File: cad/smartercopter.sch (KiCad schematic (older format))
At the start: 26 parts

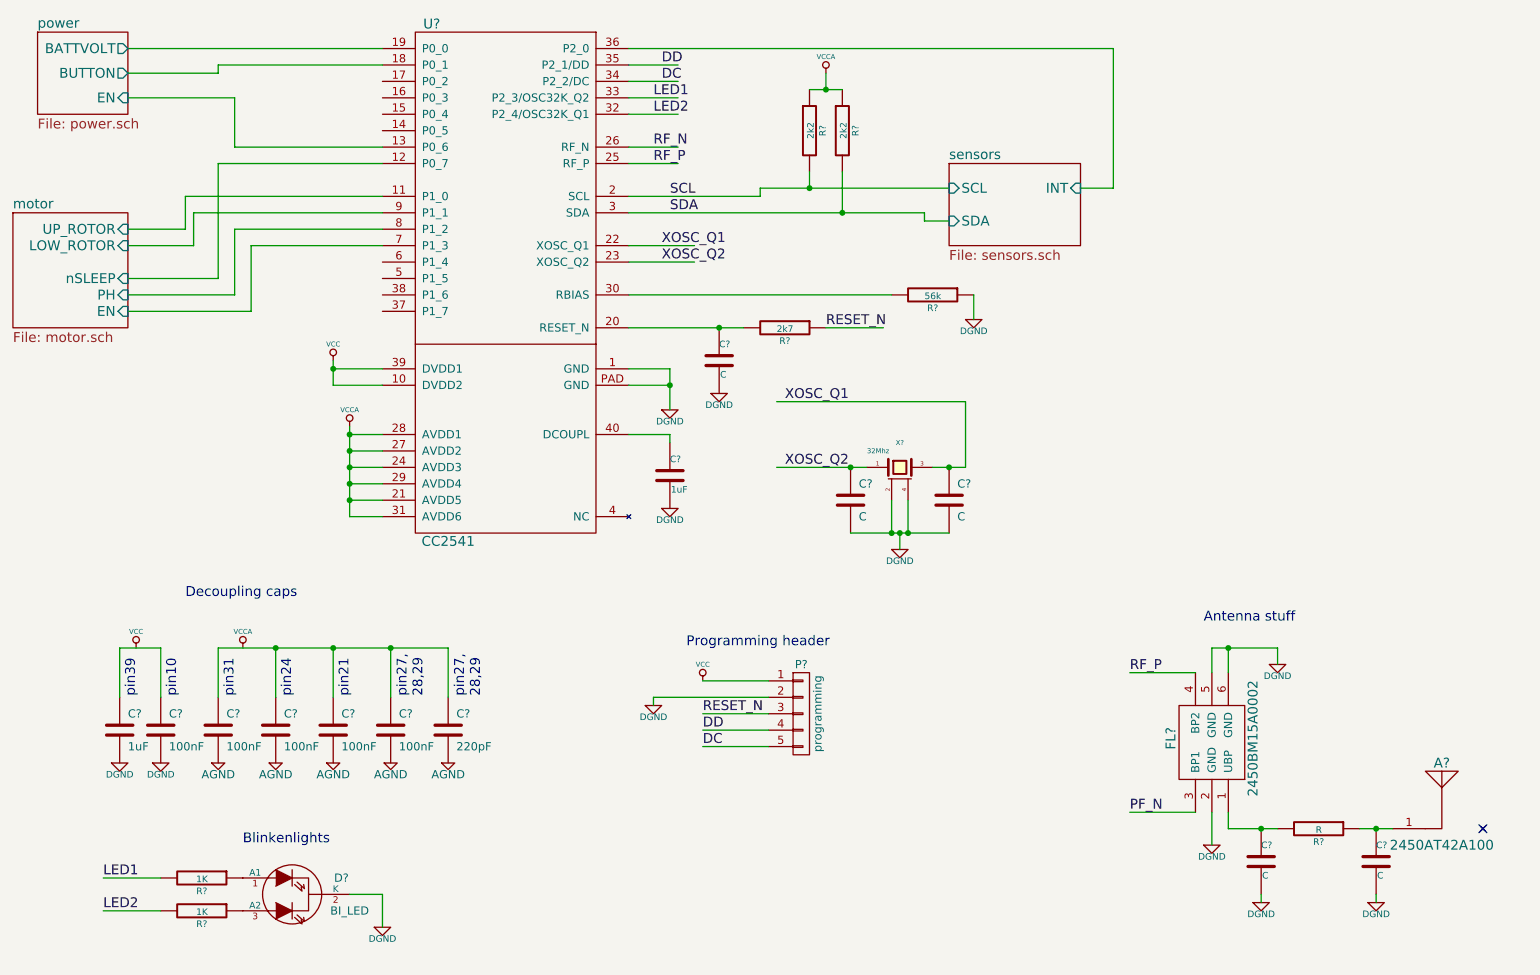
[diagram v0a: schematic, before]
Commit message: added values to crystal load caps
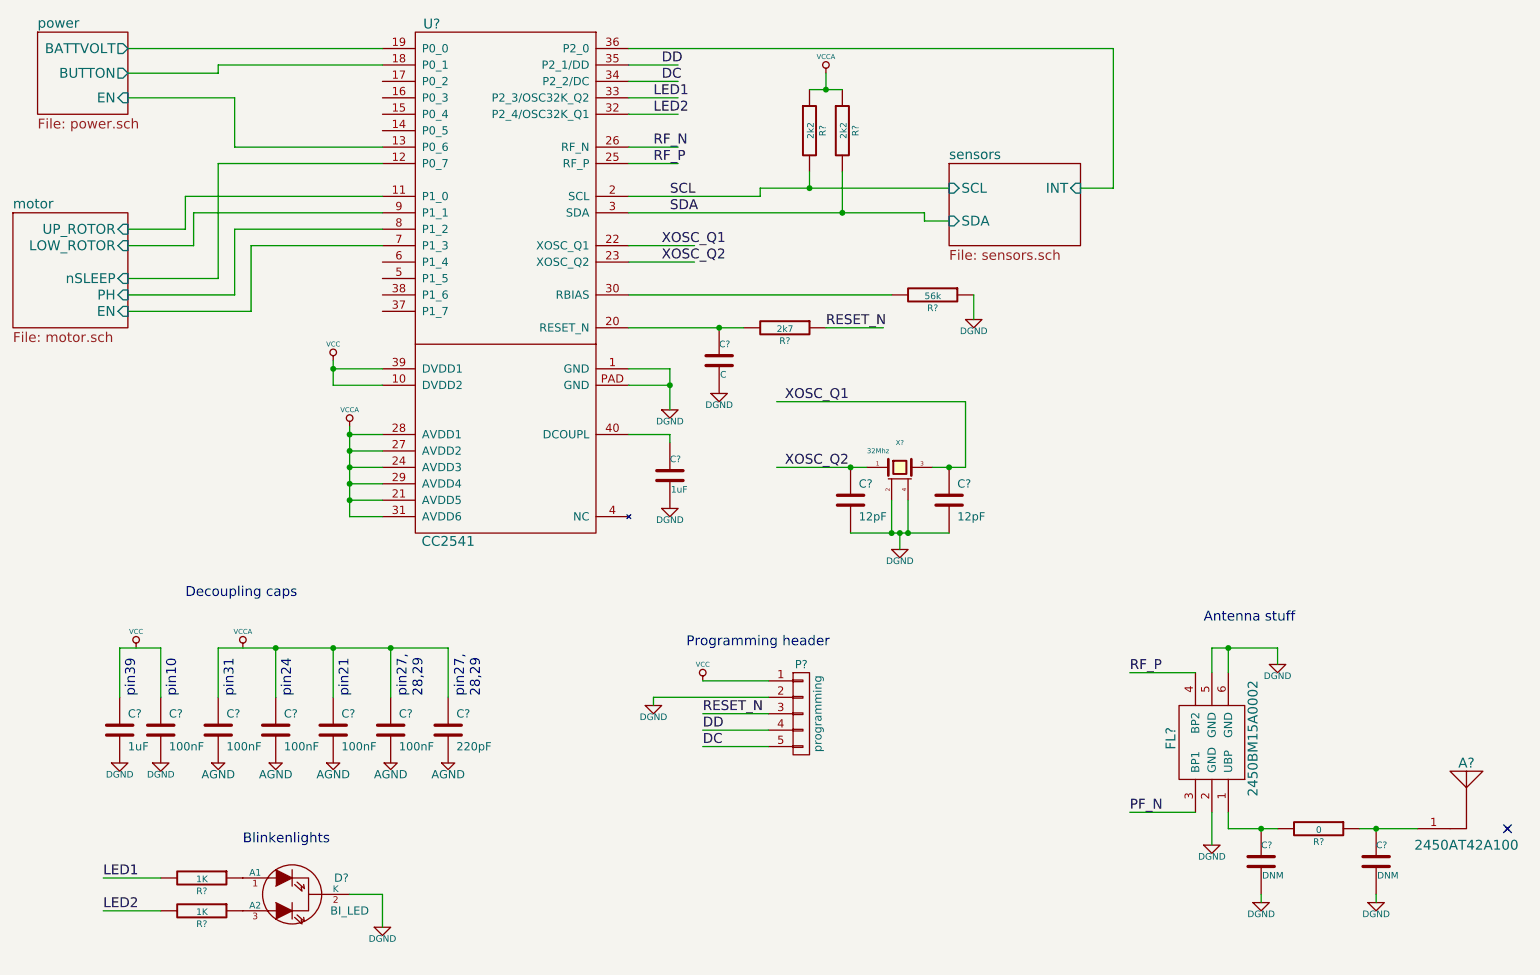
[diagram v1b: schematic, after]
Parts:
- C? (x2): value C -> 12pF
- C? (x2): value C -> DNM
- R?: value R -> 0
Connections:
- wire segments 101 -> 123
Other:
- moved on the sheet: A?
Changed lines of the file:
@@
 P 6800 4050
 F 0 "C?" H 6850 4150 50  0000 L CNN
-F 1 "C" H 6850 3950 50  0000 L CNN
+F 1 "12pF" H 6850 3950 50  0000 L CNN
 F 2 "" H 6800 4050 60  0000 C CNN
 F 3 "" H 6800 4050 60  0000 C CNN
@@
 P 6200 4050
 F 0 "C?" H 6250 4150 50  0000 L CNN
-F 1 "C" H 6250 3950 50  0000 L CNN
+F 1 "12pF" H 6250 3950 50  0000 L CNN
 F 2 "" H 6200 4050 60  0000 C CNN
 F 3 "" H 6200 4050 60  0000 C CNN
@@
 $EndComp
 Wire Wire Line
-	3150 3600 3150 4150
+	3150 3600 3150 3650
+Wire Wire Line
+	3150 3650 3150 3750
+Wire Wire Line
+	3150 3750 3150 3850
+Wire Wire Line
+	3150 3850 3150 3950
+Wire Wire Line
+	3150 3950 3150 4050
+Wire Wire Line
+	3150 4050 3150 4150
 Wire Wire Line
 	3150 4150 3350 4150
@@
 	4850 3250 5100 3250
 Wire Wire Line
-	5100 3250 5100 3500
+	5100 3250 5100 3350
+Wire Wire Line
+	5100 3350 5100 3500
 Wire Wire Line
 	4850 3350 5100 3350
 Connection ~ 5100 3350
 Wire Wire Line
-	3050 3200 3050 3350
+	3050 3200 3050 3250
+Wire Wire Line
+	3050 3250 3050 3350
 Wire Wire Line
 	4850 3650 5100 3650
@@
 	5100 3650 5100 3700
 Wire Wire Line
-	4850 3000 5550 3000
+	4850 3000 5400 3000
+Wire Wire Line
+	5400 3000 5550 3000
 Connection ~ 5400 3000
 Wire Wire Line
@@
 	6950 2800 6950 2950
 Wire Wire Line
-	6200 4250 6800 4250
+	6200 4250 6450 4250
+Wire Wire Line
+	6450 4250 6500 4250
+Wire Wire Line
+	6500 4250 6550 4250
+Wire Wire Line
+	6550 4250 6800 4250
 Wire Wire Line
 	6550 4050 6550 4250
@@
 	4850 2200 5650 2200
 Wire Wire Line
-	4850 2300 6650 2300
+	4850 2300 6150 2300
+Wire Wire Line
+	6150 2300 6650 2300
 Text Label 5100 2200 0    60   ~ 0
 SCL
@@
 XOSC_Q2
 Wire Wire Line
-	5750 3850 6300 3850
-Wire Wire Line
-	6700 3850 6900 3850
+	5750 3850 6200 3850
+Wire Wire Line
+	6200 3850 6300 3850
+Wire Wire Line
+	6700 3850 6800 3850
+Wire Wire Line
+	6800 3850 6900 3850
 Wire Wire Line
 	6900 3850 6900 3450
@@
 	2350 5250 2350 4950
 Wire Wire Line
-	2350 4950 3750 4950
+	2350 4950 2700 4950
+Wire Wire Line
+	2700 4950 3050 4950
+Wire Wire Line
+	3050 4950 3400 4950
+Wire Wire Line
+	3400 4950 3750 4950
 Wire Wire Line
 	3750 4950 3750 5250
@@
 	5650 2200 5650 2150
 Wire Wire Line
-	5650 2150 6800 2150
+	5650 2150 5950 2150
+Wire Wire Line
+	5950 2150 6800 2150
 Wire Wire Line
 	6650 2300 6650 2350
@@
 $EndComp
 Wire Wire Line
-	5950 1550 6150 1550
+	5950 1550 6050 1550
+Wire Wire Line
+	6050 1550 6150 1550
 Wire Wire Line
 	6050 1450 6050 1550
@@
 L 2450AT42A100 A?
 U 1 1 54954E38
-P 9800 6050
-F 0 "A?" H 9800 6450 60  0000 C CNN
-F 1 "2450AT42A100" H 9800 5950 60  0000 C CNN
-F 2 "" H 9800 6050 60  0000 C CNN
-F 3 "" H 9800 6050 60  0000 C CNN
-	1    9800 6050
+P 9950 6050
+F 0 "A?" H 9950 6450 60  0000 C CNN
+F 1 "2450AT42A100" H 9950 5950 60  0000 C CNN
+F 2 "" H 9950 6050 60  0000 C CNN
+F 3 "" H 9950 6050 60  0000 C CNN
+	1    9950 6050
 	1    0    0    -1
 $EndComp
@@
 P 8700 6250
 F 0 "C?" H 8700 6350 40  0000 L CNN
-F 1 "C" H 8706 6165 40  0000 L CNN
+F 1 "DNM" H 8706 6165 40  0000 L CNN
 F 2 "" H 8738 6100 30  0000 C CNN
 F 3 "" H 8700 6250 60  0000 C CNN
@@
 P 9400 6250
 F 0 "C?" H 9400 6350 40  0000 L CNN
-F 1 "C" H 9406 6165 40  0000 L CNN
+F 1 "DNM" H 9406 6165 40  0000 L CNN
 F 2 "" H 9438 6100 30  0000 C CNN
 F 3 "" H 9400 6250 60  0000 C CNN
@@
 P 9050 6050
 F 0 "R?" V 9130 6050 40  0000 C CNN
-F 1 "R" V 9057 6051 40  0000 C CNN
+F 1 "0" V 9057 6051 40  0000 C CNN
 F 2 "" V 8980 6050 30  0000 C CNN
 F 3 "" H 9050 6050 30  0000 C CNN
@@
 $EndComp
 $Comp
-L DGND #PWR?
+L DGND #PWR018
 U 1 1 5495965C
 P 8400 6150
-F 0 "#PWR?" H 8400 6150 40  0001 C CNN
+F 0 "#PWR018" H 8400 6150 40  0001 C CNN
 F 1 "DGND" H 8400 6080 40  0000 C CNN
 F 2 "" H 8400 6150 60  0000 C CNN
@@
 $EndComp
 $Comp
-L DGND #PWR?
+L DGND #PWR019
 U 1 1 549596DE
 P 9400 6500
-F 0 "#PWR?" H 9400 6500 40  0001 C CNN
+F 0 "#PWR019" H 9400 6500 40  0001 C CNN
 F 1 "DGND" H 9400 6430 40  0000 C CNN
 F 2 "" H 9400 6500 60  0000 C CNN
@@
 $EndComp
 $Comp
-L DGND #PWR?
+L DGND #PWR020
 U 1 1 54959760
 P 8800 5050
-F 0 "#PWR?" H 8800 5050 40  0001 C CNN
+F 0 "#PWR020" H 8800 5050 40  0001 C CNN
 F 1 "DGND" H 8800 4980 40  0000 C CNN
 F 2 "" H 8800 5050 60  0000 C CNN
@@
 $EndComp
 $Comp
-L DGND #PWR?
+L DGND #PWR021
 U 1 1 54959F9E
 P 8700 6500
-F 0 "#PWR?" H 8700 6500 40  0001 C CNN
+F 0 "#PWR021" H 8700 6500 40  0001 C CNN
 F 1 "DGND" H 8700 6430 40  0000 C CNN
 F 2 "" H 8700 6500 60  0000 C CNN
@@
 $EndComp
 Wire Wire Line
-	8500 6050 8800 6050
-Wire Wire Line
-	9300 6050 9500 6050
+	8500 6050 8700 6050
+Wire Wire Line
+	8700 6050 8800 6050
+Wire Wire Line
+	9300 6050 9400 6050
+Wire Wire Line
+	9400 6050 9650 6050
 Connection ~ 9400 6050
 Wire Wire Line
@@
 Wire Wire Line
 	8700 6500 8700 6450
-NoConn ~ 10050 6050
+NoConn ~ 10200 6050
 Wire Wire Line
 	8500 5950 8500 6050
@@
 	8400 5100 8400 4950
 Wire Wire Line
-	8400 4950 8800 4950
+	8400 4950 8500 4950
+Wire Wire Line
+	8500 4950 8800 4950
 Wire Wire Line
 	8800 4950 8800 5050
@@
 $EndComp
 $Comp
-L DGND #PWR?
+L DGND #PWR022
 U 1 1 549158BD
 P 3350 6650
-F 0 "#PWR?" H 3350 6650 40  0001 C CNN
+F 0 "#PWR022" H 3350 6650 40  0001 C CNN
 F 1 "DGND" H 3350 6580 40  0000 C CNN
 F 2 "" H 3350 6650 60  0000 C CNN
@@
 	5700 5450 5300 5450
 $Comp
-L VCC #PWR?
+L VCC #PWR023
 U 1 1 549191D8
 P 5300 5150
-F 0 "#PWR?" H 5300 5250 30  0001 C CNN
+F 0 "#PWR023" H 5300 5250 30  0001 C CNN
 F 1 "VCC" H 5300 5250 30  0000 C CNN
 F 2 "" H 5300 5150 60  0000 C CNN
@@
 $EndComp
 $Comp
-L DGND #PWR?
+L DGND #PWR024
 U 1 1 54919227
 P 5000 5300
-F 0 "#PWR?" H 5000 5300 40  0001 C CNN
+F 0 "#PWR024" H 5000 5300 40  0001 C CNN
 F 1 "DGND" H 5000 5230 40  0000 C CNN
 F 2 "" H 5000 5300 60  0000 C CNN

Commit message: passed erc
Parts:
- gave numbers to parts that had none: 26
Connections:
- net labels removed: PF_N
- wire segments 123 -> 101
- no-connect marks 1 -> 9
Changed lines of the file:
@@
 $EndDescr
 $Comp
-L CC2541 U?
+L CC2541 U1
 U 1 1 548BD357
 P 4100 2650
-F 0 "U?" H 3650 4150 60  0000 C CNN
+F 0 "U1" H 3650 4150 60  0000 C CNN
 F 1 "CC2541" H 3750 1000 60  0000 C CNN
 F 2 "" H 4500 1250 60  0000 C CNN
@@
 $EndSheet
 $Comp
-L C C?
+L C C8
 U 1 1 548CB6FE
 P 5100 3900
-F 0 "C?" H 5100 4000 40  0000 L CNN
+F 0 "C8" H 5100 4000 40  0000 L CNN
 F 1 "1uF" H 5106 3815 40  0000 L CNN
 F 2 "" H 5138 3750 30  0000 C CNN
@@
 $EndComp
 $Comp
-L C C?
+L C C9
 U 1 1 548CC96E
 P 5400 3200
-F 0 "C?" H 5400 3300 40  0000 L CNN
+F 0 "C9" H 5400 3300 40  0000 L CNN
 F 1 "C" H 5406 3115 40  0000 L CNN
 F 2 "" H 5438 3050 30  0000 C CNN
@@
 $EndComp
 $Comp
-L R R?
+L R R3
 U 1 1 548CCA9E
 P 5800 3000
-F 0 "R?" V 5880 3000 40  0000 C CNN
+F 0 "R3" V 5880 3000 40  0000 C CNN
 F 1 "2k7" V 5807 3001 40  0000 C CNN
 F 2 "" V 5730 3000 30  0000 C CNN
@@
 RESET_N
 $Comp
-L R R?
+L R R6
 U 1 1 548CCFA8
 P 6700 2800
-F 0 "R?" V 6780 2800 40  0000 C CNN
+F 0 "R6" V 6780 2800 40  0000 C CNN
 F 1 "56k" V 6707 2801 40  0000 C CNN
 F 2 "" V 6630 2800 30  0000 C CNN
@@
 $EndComp
 $Comp
-L C C?
+L C C11
 U 1 1 548CD35A
 P 6800 4050
-F 0 "C?" H 6850 4150 50  0000 L CNN
+F 0 "C11" H 6850 4150 50  0000 L CNN
 F 1 "12pF" H 6850 3950 50  0000 L CNN
 F 2 "" H 6800 4050 60  0000 C CNN
@@
 $EndComp
 $Comp
-L C C?
+L C C10
 U 1 1 548CD39E
 P 6200 4050
-F 0 "C?" H 6250 4150 50  0000 L CNN
+F 0 "C10" H 6250 4150 50  0000 L CNN
 F 1 "12pF" H 6250 3950 50  0000 L CNN
 F 2 "" H 6200 4050 60  0000 C CNN
@@
 $EndComp
 Wire Wire Line
-	3150 3600 3150 3650
-Wire Wire Line
-	3150 3650 3150 3750
-Wire Wire Line
-	3150 3750 3150 3850
-Wire Wire Line
-	3150 3850 3150 3950
-Wire Wire Line
-	3150 3950 3150 4050
-Wire Wire Line
-	3150 4050 3150 4150
+	3150 3600 3150 4150
 Wire Wire Line
 	3150 4150 3350 4150
@@
 	4850 3250 5100 3250
 Wire Wire Line
-	5100 3250 5100 3350
-Wire Wire Line
-	5100 3350 5100 3500
+	5100 3250 5100 3500
 Wire Wire Line
 	4850 3350 5100 3350
 Connection ~ 5100 3350
 Wire Wire Line
-	3050 3200 3050 3250
-Wire Wire Line
-	3050 3250 3050 3350
+	3050 3200 3050 3350
 Wire Wire Line
 	4850 3650 5100 3650
@@
 	5100 3650 5100 3700
 Wire Wire Line
-	4850 3000 5400 3000
-Wire Wire Line
-	5400 3000 5550 3000
+	4850 3000 5550 3000
 Connection ~ 5400 3000
 Wire Wire Line
@@
 	6950 2800 6950 2950
 Wire Wire Line
-	6200 4250 6450 4250
-Wire Wire Line
-	6450 4250 6500 4250
-Wire Wire Line
-	6500 4250 6550 4250
-Wire Wire Line
-	6550 4250 6800 4250
+	6200 4250 6800 4250
 Wire Wire Line
 	6550 4050 6550 4250
@@
 	4850 2200 5650 2200
 Wire Wire Line
-	4850 2300 6150 2300
-Wire Wire Line
-	6150 2300 6650 2300
+	4850 2300 6650 2300
 Text Label 5100 2200 0    60   ~ 0
 SCL
@@
 XOSC_Q2
 Wire Wire Line
-	5750 3850 6200 3850
-Wire Wire Line
-	6200 3850 6300 3850
-Wire Wire Line
-	6700 3850 6800 3850
-Wire Wire Line
-	6800 3850 6900 3850
+	5750 3850 6300 3850
+Wire Wire Line
+	6700 3850 6900 3850
 Wire Wire Line
 	6900 3850 6900 3450
@@
 XOSC_Q2
 $Comp
-L C C?
+L C C1
 U 1 1 548D168D
 P 1750 5450
-F 0 "C?" H 1800 5550 50  0000 L CNN
+F 0 "C1" H 1800 5550 50  0000 L CNN
 F 1 "1uF" H 1800 5350 50  0000 L CNN
 F 2 "" H 1750 5450 60  0000 C CNN
@@
 $EndComp
 $Comp
-L C C?
+L C C2
 U 1 1 548D1805
 P 2000 5450
-F 0 "C?" H 2050 5550 50  0000 L CNN
+F 0 "C2" H 2050 5550 50  0000 L CNN
 F 1 "100nF" H 2050 5350 50  0000 L CNN
 F 2 "" H 2000 5450 60  0000 C CNN
@@
 $EndComp
 $Comp
-L C C?
+L C C3
 U 1 1 548D182C
 P 2350 5450
-F 0 "C?" H 2400 5550 50  0000 L CNN
+F 0 "C3" H 2400 5550 50  0000 L CNN
 F 1 "100nF" H 2400 5350 50  0000 L CNN
 F 2 "" H 2350 5450 60  0000 C CNN
@@
 $EndComp
 $Comp
-L C C?
+L C C4
 U 1 1 548D1892
 P 2700 5450
-F 0 "C?" H 2750 5550 50  0000 L CNN
+F 0 "C4" H 2750 5550 50  0000 L CNN
 F 1 "100nF" H 2750 5350 50  0000 L CNN
 F 2 "" H 2700 5450 60  0000 C CNN
@@
 $EndComp
 $Comp
-L C C?
+L C C5
 U 1 1 548D18DD
 P 3050 5450
-F 0 "C?" H 3100 5550 50  0000 L CNN
+F 0 "C5" H 3100 5550 50  0000 L CNN
 F 1 "100nF" H 3100 5350 50  0000 L CNN
 F 2 "" H 3050 5450 60  0000 C CNN
@@
 $EndComp
 $Comp
-L C C?
+L C C6
 U 1 1 548D1913
 P 3400 5450
-F 0 "C?" H 3450 5550 50  0000 L CNN
+F 0 "C6" H 3450 5550 50  0000 L CNN
 F 1 "100nF" H 3450 5350 50  0000 L CNN
 F 2 "" H 3400 5450 60  0000 C CNN
@@
 $EndComp
 $Comp
-L C C?
+L C C7
 U 1 1 548D1948
 P 3750 5450
-F 0 "C?" H 3800 5550 50  0000 L CNN
+F 0 "C7" H 3800 5550 50  0000 L CNN
 F 1 "220pF" H 3800 5350 50  0000 L CNN
 F 2 "" H 3750 5450 60  0000 C CNN
@@
 	2350 5250 2350 4950
 Wire Wire Line
-	2350 4950 2700 4950
-Wire Wire Line
-	2700 4950 3050 4950
-Wire Wire Line
-	3050 4950 3400 4950
-Wire Wire Line
-	3400 4950 3750 4950
+	2350 4950 3750 4950
 Wire Wire Line
 	3750 4950 3750 5250
@@
 	5650 2200 5650 2150
 Wire Wire Line
-	5650 2150 5950 2150
-Wire Wire Line
-	5950 2150 6800 2150
+	5650 2150 6800 2150
 Wire Wire Line
 	6650 2300 6650 2350
@@
 	6650 2350 6800 2350
 $Comp
-L R R?
+L R R4
 U 1 1 549350E6
 P 5950 1800
-F 0 "R?" V 6030 1800 40  0000 C CNN
+F 0 "R4" V 6030 1800 40  0000 C CNN
 F 1 "2k2" V 5957 1801 40  0000 C CNN
 F 2 "" V 5880 1800 30  0000 C CNN
@@
 $EndComp
 $Comp
-L R R?
+L R R5
 U 1 1 5493575D
 P 6150 1800
-F 0 "R?" V 6230 1800 40  0000 C CNN
+F 0 "R5" V 6230 1800 40  0000 C CNN
 F 1 "2k2" V 6157 1801 40  0000 C CNN
 F 2 "" V 6080 1800 30  0000 C CNN
@@
 $EndComp
 Wire Wire Line
-	5950 1550 6050 1550
-Wire Wire Line
-	6050 1550 6150 1550
+	5950 1550 6150 1550
 Wire Wire Line
 	6050 1450 6050 1550
@@
 	7800 2150 7600 2150
 $Comp
-L CRYSTAL_SMD_2GND X?
+L CRYSTAL_SMD_2GND X1
 U 1 1 54948988
 P 6500 3850
-F 0 "X?" H 6500 4000 30  0000 C CNN
+F 0 "X1" H 6500 4000 30  0000 C CNN
 F 1 "32Mhz" H 6300 3950 30  0000 L CNN
 F 2 "" H 6500 3850 60  0000 C CNN
@@
 	1800 2900 2550 2900
 $Comp
-L 2450BM15A0002 FL?
+L 2450BM15A0002 FL1
 U 1 1 54954D1C
 P 8400 5550
-F 0 "FL?" H 8450 5800 60  0000 C CNN
+F 0 "FL1" H 8450 5800 60  0000 C CNN
 F 1 "2450BM15A0002" H 8450 5300 60  0000 C CNN
 F 2 "" H 8500 5350 60  0000 C CNN
@@
 $EndComp
 $Comp
-L 2450AT42A100 A?
+L 2450AT42A100 A1
 U 1 1 54954E38
 P 9950 6050
-F 0 "A?" H 9950 6450 60  0000 C CNN
+F 0 "A1" H 9950 6450 60  0000 C CNN
 F 1 "2450AT42A100" H 9950 5950 60  0000 C CNN
 F 2 "" H 9950 6050 60  0000 C CNN
@@
 RF_P
 Text Label 7900 5950 0    60   ~ 0
-PF_N
-$Comp
-L C C?
+RF_N
+$Comp
+L C C12
 U 1 1 54959458
 P 8700 6250
-F 0 "C?" H 8700 6350 40  0000 L CNN
+F 0 "C12" H 8700 6350 40  0000 L CNN
 F 1 "DNM" H 8706 6165 40  0000 L CNN
 F 2 "" H 8738 6100 30  0000 C CNN
@@
 $EndComp
 $Comp
-L C C?
+L C C13
 U 1 1 549594ED
 P 9400 6250
-F 0 "C?" H 9400 6350 40  0000 L CNN
+F 0 "C13" H 9400 6350 40  0000 L CNN
 F 1 "DNM" H 9406 6165 40  0000 L CNN
 F 2 "" H 9438 6100 30  0000 C CNN
@@
 $EndComp
 $Comp
-L R R?
+L R R7
 U 1 1 5495957A
 P 9050 6050
-F 0 "R?" V 9130 6050 40  0000 C CNN
+F 0 "R7" V 9130 6050 40  0000 C CNN
 F 1 "0" V 9057 6051 40  0000 C CNN
 F 2 "" V 8980 6050 30  0000 C CNN
@@
 $EndComp
 Wire Wire Line
-	8500 6050 8700 6050
-Wire Wire Line
-	8700 6050 8800 6050
-Wire Wire Line
-	9300 6050 9400 6050
-Wire Wire Line
-	9400 6050 9650 6050
+	8500 6050 8800 6050
+Wire Wire Line
+	9300 6050 9650 6050
 Connection ~ 9400 6050
 Wire Wire Line
@@
 	8400 5100 8400 4950
 Wire Wire Line
-	8400 4950 8500 4950
-Wire Wire Line
-	8500 4950 8800 4950
+	8400 4950 8800 4950
 Wire Wire Line
 	8800 4950 8800 5050
@@
 LED2
 $Comp
-L R R?
+L R R1
 U 1 1 5491496C
 P 2250 6350
-F 0 "R?" V 2330 6350 40  0000 C CNN
+F 0 "R1" V 2330 6350 40  0000 C CNN
 F 1 "1K" V 2257 6351 40  0000 C CNN
 F 2 "" V 2180 6350 30  0000 C CNN
@@
 $EndComp
 $Comp
-L BI_LED D?
+L BI_LED D1
 U 1 1 549157A0
 P 2800 6450
-F 0 "D?" H 3100 6550 50  0000 C CNN
+F 0 "D1" H 3100 6550 50  0000 C CNN
 F 1 "BI_LED" H 3150 6350 50  0000 C CNN
 F 2 "" H 2800 6450 60  0000 C CNN
@@
 $EndComp
 $Comp
-L R R?
+L R R2
 U 1 1 54915854
 P 2250 6550
-F 0 "R?" V 2330 6550 40  0000 C CNN
+F 0 "R2" V 2330 6550 40  0000 C CNN
 F 1 "1K" V 2257 6551 40  0000 C CNN
 F 2 "" V 2180 6550 30  0000 C CNN
@@
 LED2
 $Comp
-L CONN_01X05 P?
+L CONN_01X05 P1
 U 1 1 5491875F
 P 5900 5350
-F 0 "P?" H 5900 5650 50  0000 C CNN
+F 0 "P1" H 5900 5650 50  0000 C CNN
 F 1 "programming" V 6000 5350 50  0000 C CNN
 F 2 "" H 5900 5350 60  0000 C CNN
@@
 Text Notes 2150 4650 0    60   ~ 0
 Decoupling caps
+NoConn ~ 3350 1500
+NoConn ~ 3350 1600
+NoConn ~ 3350 1700
+NoConn ~ 3350 1800
+NoConn ~ 3350 2600
+NoConn ~ 3350 2700
+NoConn ~ 3350 2800
+NoConn ~ 3350 2900
 $EndSCHEMATC

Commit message: did stuff here, not exactly sure what
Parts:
- C2: MPN (none) -> LMK105BJ104KV-F
- C9: value C -> 1nF
- P1: value programming -> CONN_5
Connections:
- no-connect marks 9 -> 8
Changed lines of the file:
@@
 P 5400 3200
 F 0 "C9" H 5400 3300 40  0000 L CNN
-F 1 "C" H 5406 3115 40  0000 L CNN
+F 1 "1nF" H 5406 3115 40  0000 L CNN
 F 2 "" H 5438 3050 30  0000 C CNN
 F 3 "" H 5400 3200 60  0000 C CNN
@@
 F 2 "" H 2000 5450 60  0000 C CNN
 F 3 "" H 2000 5450 60  0000 C CNN
+F 4 "LMK105BJ104KV-F" H 2000 5450 60  0001 C CNN "MPN"
 	1    2000 5450
 	1    0    0    -1
@@
 Wire Wire Line
 	8700 6500 8700 6450
-NoConn ~ 10200 6050
 Wire Wire Line
 	8500 5950 8500 6050
@@
 P 5900 5350
 F 0 "P1" H 5900 5650 50  0000 C CNN
-F 1 "programming" V 6000 5350 50  0000 C CNN
+F 1 "CONN_5" V 6000 5350 50  0000 C CNN
 F 2 "" H 5900 5350 60  0000 C CNN
 F 3 "" H 5900 5350 60  0000 C CNN

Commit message: added more stuff to bom
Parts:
- A1: MPN (none) -> 2450AT42A100
- C1: MPN (none) -> GRM155R60J105KE19D
- C10: MPN (none) -> 02013A120JAT2A
- FL1: MPN (none) -> 2450BM15A0002
- X1: MPN (none) -> FA-128 32MHz 10pF 10PPM
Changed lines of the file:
@@
 F 2 "" H 6200 4050 60  0000 C CNN
 F 3 "" H 6200 4050 60  0000 C CNN
+F 4 "02013A120JAT2A" H 6200 4050 60  0001 C CNN "MPN"
 	1    6200 4050
 	1    0    0    -1
@@
 F 2 "" H 1750 5450 60  0000 C CNN
 F 3 "" H 1750 5450 60  0000 C CNN
+F 4 "GRM155R60J105KE19D" H 1750 5450 60  0001 C CNN "MPN"
 	1    1750 5450
 	1    0    0    -1
@@
 F 2 "" H 6500 3850 60  0000 C CNN
 F 3 "" H 6500 3850 60  0000 C CNN
+F 4 "FA-128 32MHz 10pF 10PPM" H 6500 3850 60  0001 C CNN "MPN"
 	1    6500 3850
 	1    0    0    -1
@@
 F 2 "" H 8500 5350 60  0000 C CNN
 F 3 "" H 8500 5350 60  0000 C CNN
+F 4 "2450BM15A0002" H 8400 5550 60  0001 C CNN "MPN"
 	1    8400 5550
 	0    -1   -1   0
@@
 F 2 "" H 9950 6050 60  0000 C CNN
 F 3 "" H 9950 6050 60  0000 C CNN
+F 4 "2450AT42A100" H 9950 6050 60  0001 C CNN "MPN"
 	1    9950 6050
 	1    0    0    -1
